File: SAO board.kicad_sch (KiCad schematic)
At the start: 40 parts, among them J1 5V, SW1 SW_SPDT, U1 MIC5219-3.3YM5, U2 MIC5219-3.3YM5, U3 MIC5219-3.3YM5, U4 MIC5219-3.3YM5, U5 MIC5219-3.3YM5

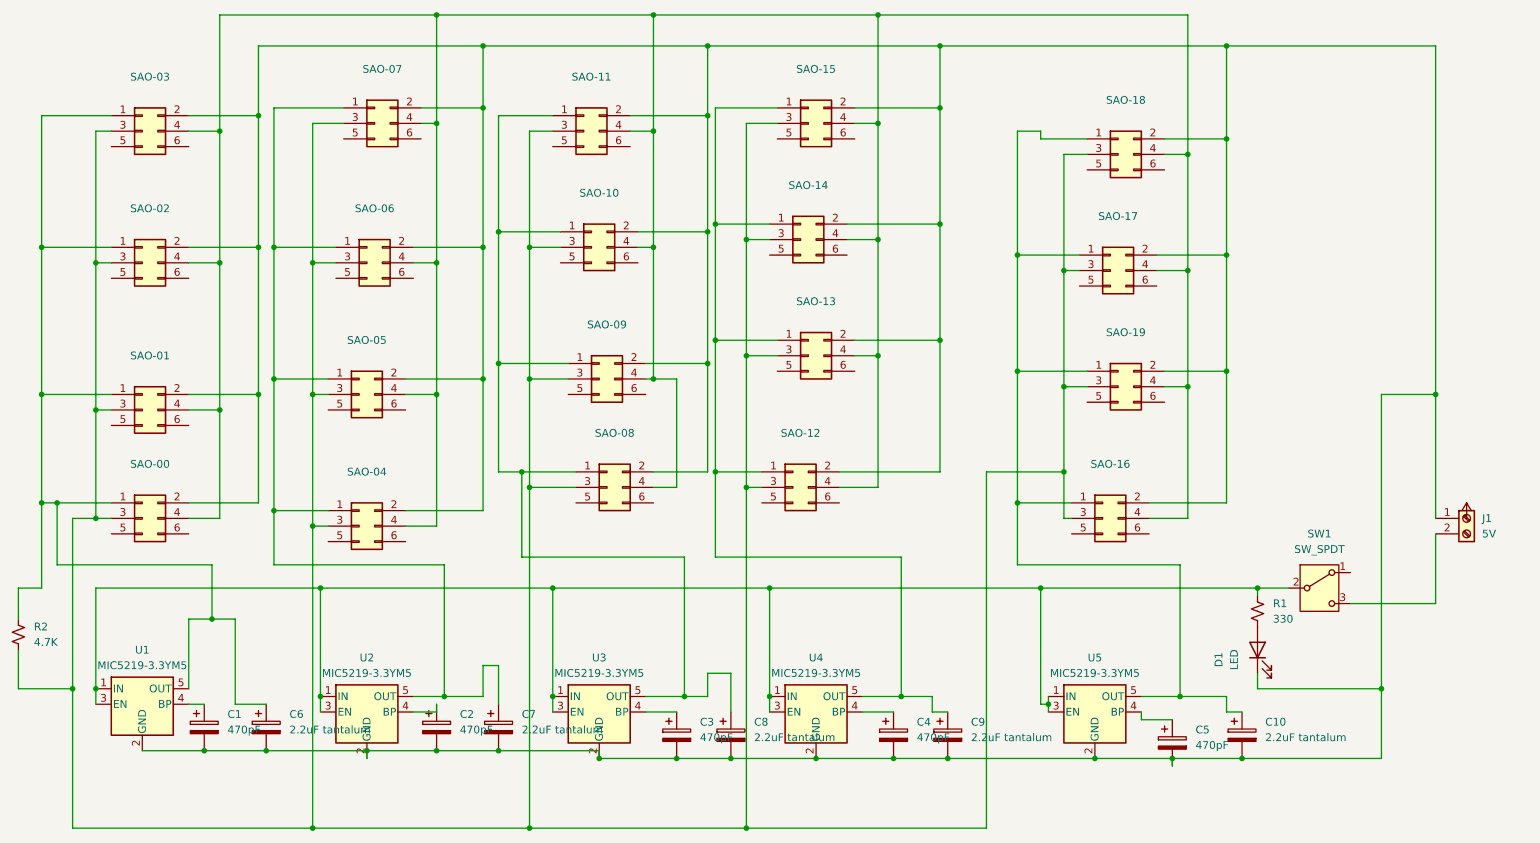
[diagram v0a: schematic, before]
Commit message: updated circuit and layout
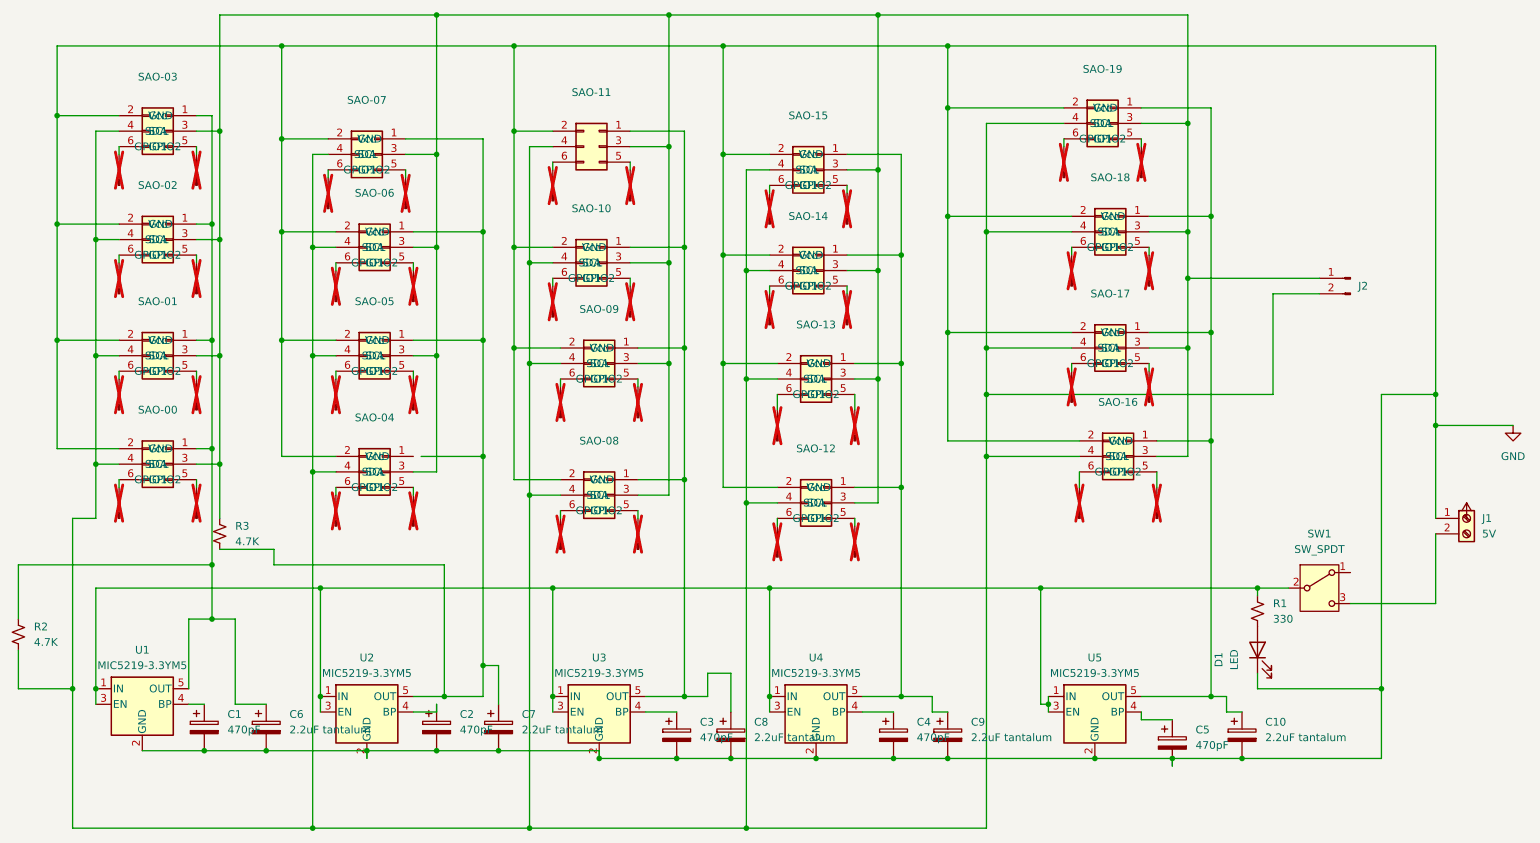
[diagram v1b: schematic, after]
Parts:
- removed SAO-00, SAO-01, SAO-02, SAO-04, SAO-05, SAO-06, SAO-07, SAO-08, SAO-09, SAO-10, SAO-11, SAO-12, SAO-13, SAO-14, SAO-15, SAO-16, SAO-17, SAO-18, SAO-19: Conn_02x03_Odd_Even, Connector_PinHeader_1.00mm:PinHeader_2x03_P1.00mm_Vertical, symbol Connector_Generic:Conn_02x03_Odd_Even
- removed SAO-03: ~, Connector_PinHeader_1.00mm:PinHeader_2x03_P1.00mm_Vertical, symbol Connector_Generic:Conn_02x03_Odd_Even
- added J10, J11, J12, J13, J14, J15, J16, J17, J18, J19, J20, J21, J22, J23, J24, J25, J26, J27, J28, J29, J3, J30, J31, J32, J33, J34, J35, J36, J37, J38, J39, J4, J40, J41, J42, J5, J6, J7, J8, J9: Conn_01x01_Pin, Connector_PinHeader_2.54mm:PinHeader_1x01_P2.54mm_Horizontal, symbol Connector:Conn_01x01_Pin
- added J2: ~, Connector_PinHeader_2.54mm:PinHeader_1x02_P2.54mm_Vertical, symbol Connector:Conn_01x02_Pin
- added R3: 4.7K, Inductor_SMD:L_1008_2520Metric, symbol Device:R_Small_US
- added SAO-00, SAO-01, SAO-02, SAO-03, SAO-04, SAO-05, SAO-06, SAO-07, SAO-08, SAO-09, SAO-10, SAO-11, SAO-12, SAO-13, SAO-14, SAO-15, SAO-16, SAO-17, SAO-18, SAO-19: SAO, Connector_PinHeader_2.54mm:PinHeader_2x03_P2.54mm_Vertical, symbol SAO:SAO
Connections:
- net GND: now reaches C1.2, C10.2, C2.2, C3.2, C4.2, C5.2, C6.2, C7.2, C8.2, C9.2, D1.1 (K), J1.1 (Pin_1), U1.2 (GND), U2.2 (GND), U3.2 (GND), U4.2 (GND), U5.2 (GND)
- net GND: now also SAO-00.2 (GND), SAO-01.2 (GND), SAO-02.2 (GND), SAO-03.2 (GND), SAO-04.2 (GND), SAO-05.2 (GND), SAO-06.2 (GND), SAO-07.2 (GND), SAO-08.2 (GND), SAO-09.2 (GND), SAO-10.2 (GND), SAO-11.2 (GND), SAO-12.2 (GND), SAO-13.2 (GND), SAO-14.2 (GND), SAO-15.2 (GND), SAO-16.2 (GND), SAO-17.2 (GND), SAO-18.2 (GND), SAO-19.2 (GND)
- net at C6.1, R2.1, U1.5 (OUT): now also SAO-00.1 (Vcc), SAO-01.1 (Vcc), SAO-02.1 (Vcc), SAO-03.1 (Vcc)
- net at C8.1, U3.5 (OUT): now also SAO-08.1 (Vcc), SAO-09.1 (Vcc), SAO-10.1 (Vcc), SAO-11.1 (Vcc)
- net at C9.1, U4.5 (OUT): now also SAO-12.1 (Vcc), SAO-13.1 (Vcc), SAO-14.1 (Vcc), SAO-15.1 (Vcc)
- net at R2.2: now also J2.2 (Pin_2), SAO-00.4 (SCL), SAO-01.4 (SCL), SAO-02.4 (SCL), SAO-03.4 (SCL), SAO-04.4 (SCL), SAO-05.4 (SCL), SAO-06.4 (SCL), SAO-07.4 (SCL), SAO-08.4 (SCL), SAO-09.4 (SCL), SAO-10.4 (SCL), SAO-11.4 (SCL), SAO-12.4 (SCL), SAO-13.4 (SCL), SAO-14.4 (SCL), SAO-15.4 (SCL), SAO-16.4 (SCL), SAO-17.4 (SCL), SAO-18.4 (SCL), SAO-19.4 (SCL)
- net at C7.1, U2.5 (OUT): now also R3.2, SAO-05.1 (Vcc), SAO-06.1 (Vcc), SAO-07.1 (Vcc)
- net at C10.1, U5.5 (OUT): now also SAO-16.1 (Vcc), SAO-17.1 (Vcc), SAO-18.1 (Vcc), SAO-19.1 (Vcc)
- new net: J23.1 (Pin_1), SAO-10.6 (GPIO2)
- new net: J2.1 (Pin_1), R3.1, SAO-00.3 (SDA), SAO-01.3 (SDA), SAO-02.3 (SDA), SAO-03.3 (SDA), SAO-04.3 (SDA), SAO-05.3 (SDA), SAO-06.3 (SDA), SAO-07.3 (SDA), SAO-08.3 (SDA), SAO-09.3 (SDA), SAO-10.3 (SDA), SAO-11.3 (SDA), SAO-12.3 (SDA), SAO-13.3 (SDA), SAO-14.3 (SDA), SAO-15.3 (SDA), SAO-16.3 (SDA), SAO-17.3 (SDA), SAO-18.3 (SDA), SAO-19.3 (SDA)
- new net: J40.1 (Pin_1), SAO-17.5 (GPIO1)
- new net: J39.1 (Pin_1), SAO-17.6 (GPIO2)
- new net: J24.1 (Pin_1), SAO-10.5 (GPIO1)
- new net: J35.1 (Pin_1), SAO-19.6 (GPIO2)
- new net: J16.1 (Pin_1), SAO-05.5 (GPIO1)
- new net: J15.1 (Pin_1), SAO-05.6 (GPIO2)
- new net: J4.1 (Pin_1), SAO-03.6 (GPIO2)
- new net: J12.1 (Pin_1), SAO-07.5 (GPIO1)
- new net: J13.1 (Pin_1), SAO-06.5 (GPIO1)
- new net: J37.1 (Pin_1), SAO-18.5 (GPIO1)
- new net: J42.1 (Pin_1), SAO-16.5 (GPIO1)
- new net: J29.1 (Pin_1), SAO-14.5 (GPIO1)
- new net: J31.1 (Pin_1), SAO-13.5 (GPIO1)
- new net: J32.1 (Pin_1), SAO-13.6 (GPIO2)
- new net: J38.1 (Pin_1), SAO-18.6 (GPIO2)
- new net: J21.1 (Pin_1), SAO-09.5 (GPIO1)
- new net: J22.1 (Pin_1), SAO-09.6 (GPIO2)
- new net: J6.1 (Pin_1), SAO-02.5 (GPIO1)
- new net: J34.1 (Pin_1), SAO-12.5 (GPIO1)
- new net: J41.1 (Pin_1), SAO-16.6 (GPIO2)
- new net: J25.1 (Pin_1), SAO-11.5 (GPIO1)
- new net: J5.1 (Pin_1), SAO-02.6 (GPIO2)
- new net: J7.1 (Pin_1), SAO-01.5 (GPIO1)
- new net: J28.1 (Pin_1), SAO-15.5 (GPIO1)
- new net: J27.1 (Pin_1), SAO-15.6 (GPIO2)
- new net: J3.1 (Pin_1), SAO-03.5 (GPIO1)
- new net: J14.1 (Pin_1), SAO-06.6 (GPIO2)
- new net: J36.1 (Pin_1), SAO-19.5 (GPIO1)
- new net: J18.1 (Pin_1), SAO-04.6 (GPIO2)
- new net: J19.1 (Pin_1), SAO-08.6 (GPIO2)
- new net: J11.1 (Pin_1), SAO-07.6 (GPIO2)
- new net: J17.1 (Pin_1), SAO-04.5 (GPIO1)
- new net: J10.1 (Pin_1), SAO-00.5 (GPIO1)
- new net: J9.1 (Pin_1), SAO-00.6 (GPIO2)
- new net: J8.1 (Pin_1), SAO-01.6 (GPIO2)
- new net: J20.1 (Pin_1), SAO-08.5 (GPIO1)
- new net: J33.1 (Pin_1), SAO-12.6 (GPIO2)
- new net: J30.1 (Pin_1), SAO-14.6 (GPIO2)
- new net: J26.1 (Pin_1), SAO-11.6 (GPIO2)
